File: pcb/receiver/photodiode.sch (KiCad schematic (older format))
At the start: 111 parts, among them Q201 Q_NJFET_DGS, Q202 Q_NPN_BCE, Q203 Q_NPN_BCE, Q204 Q_NPN_BCE, Q205 Q_NPN_BCE, Q206 Q_NPN_BCE, Q207 Q_NJFET_DGS, U201 ADR550ARTZ-REEL7, U202 TL974IPWR, U203 MAX4477AUA+, U204 OPA2141AIDR, U205 NLAS4599DFT2G

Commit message: Most parts footprinted; TODO analog voltage reference, photodiodes, passives
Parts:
- U202: footprint (none) -> receiver-footprints:TI-SOIC14
- U203: footprint (none) -> receiver-footprints:Maxim-uMAX8
- U204: footprint (none) -> receiver-footprints:TI-SOIC8
- U205: footprint Package_DIP:DIP-8_W7.62mm -> receiver-footprints:On-SOT363
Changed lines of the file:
@@
 F 0 "U203" H 4300 3400 50  0000 L CNN
 F 1 "MAX4477AUA+" H 4300 3000 50  0000 L CNN
-F 2 "" H 4300 3200 50  0001 C CNN
+F 2 "receiver-footprints:Maxim-uMAX8" H 4300 3200 50  0001 C CNN
 F 3 "" H 4300 3200 50  0001 C CNN
 	1    4300 3200
@@
 F 0 "U203" H 5950 3500 50  0000 L CNN
 F 1 "MAX4477AUA+" H 5950 3100 50  0000 L CNN
-F 2 "" H 5950 3300 50  0001 C CNN
+F 2 "receiver-footprints:Maxim-uMAX8" H 5950 3300 50  0001 C CNN
 F 3 "" H 5950 3300 50  0001 C CNN
 	2    5950 3300
@@
 F 0 "U204" H 8050 3600 50  0000 L CNN
 F 1 "OPA2141AIDR" H 8050 3200 50  0000 L CNN
-F 2 "" H 8050 3400 50  0001 C CNN
+F 2 "receiver-footprints:TI-SOIC8" H 8050 3400 50  0001 C CNN
 F 3 "" H 8050 3400 50  0001 C CNN
 	1    8050 3400
@@
 F 0 "U204" H 10050 3700 50  0000 L CNN
 F 1 "OPA2141AIDR" H 10050 3300 50  0000 L CNN
-F 2 "" H 10050 3500 50  0001 C CNN
+F 2 "receiver-footprints:TI-SOIC8" H 10050 3500 50  0001 C CNN
 F 3 "" H 10050 3500 50  0001 C CNN
 	2    10050 3500
@@
 F 0 "U202" H 7300 1450 50  0000 L CNN
 F 1 "TL974IPWR" H 7300 1050 50  0000 L CNN
-F 2 "" H 7250 1350 50  0001 C CNN
+F 2 "receiver-footprints:TI-SOIC14" H 7250 1350 50  0001 C CNN
 F 3 "http://www.ti.com/lit/ds/symlink/lm2902-n.pdf" H 7350 1450 50  0001 C CNN
 	1    7300 1250
@@
 F 0 "U202" H 6750 2100 50  0000 L CNN
 F 1 "TL974IPWR" H 6750 1700 50  0000 L CNN
-F 2 "" H 6700 2000 50  0001 C CNN
+F 2 "receiver-footprints:TI-SOIC14" H 6700 2000 50  0001 C CNN
 F 3 "http://www.ti.com/lit/ds/symlink/lm2902-n.pdf" H 6800 2100 50  0001 C CNN
 	2    6750 1900
@@
 F 0 "U205" H 9775 2235 50  0000 L CNN
 F 1 "NLAS4599DFT2G" H 9775 2165 50  0000 L CNN
-F 2 "Package_DIP:DIP-8_W7.62mm" H 9900 1750 50  0001 C CNN
+F 2 "receiver-footprints:On-SOT363" H 9900 1750 50  0001 C CNN
 F 3 "https://datasheets.maximintegrated.com/en/ds/DG417-DG419.pdf" H 9900 1850 50  0001 C CNN
 	1    9900 2050
@@
 F 0 "U203" H 9450 5800 50  0000 L CNN
 F 1 "MAX4477AUA+" H 9450 5400 50  0000 L CNN
-F 2 "" H 9450 5600 50  0001 C CNN
+F 2 "receiver-footprints:Maxim-uMAX8" H 9450 5600 50  0001 C CNN
 F 3 "" H 9450 5600 50  0001 C CNN
 	3    9450 5600
@@
 F 0 "U204" H 10300 5850 50  0000 L CNN
 F 1 "OPA2141AIDR" H 10300 5450 50  0000 L CNN
-F 2 "" H 10300 5650 50  0001 C CNN
+F 2 "receiver-footprints:TI-SOIC8" H 10300 5650 50  0001 C CNN
 F 3 "" H 10300 5650 50  0001 C CNN
 	3    10300 5650
@@
 F 0 "U205" H 8775 5685 50  0000 L CNN
 F 1 "NLAS4599DFT2G" H 8775 5615 50  0000 L CNN
-F 2 "Package_DIP:DIP-8_W7.62mm" H 8900 5200 50  0001 C CNN
+F 2 "receiver-footprints:On-SOT363" H 8900 5200 50  0001 C CNN
 F 3 "https://datasheets.maximintegrated.com/en/ds/DG417-DG419.pdf" H 8900 5300 50  0001 C CNN
 	2    8900 5500
@@
 F 0 "U202" H 7600 6050 50  0000 L CNN
 F 1 "TL974IPWR" H 7600 5650 50  0000 L CNN
-F 2 "" H 7550 5950 50  0001 C CNN
+F 2 "receiver-footprints:TI-SOIC14" H 7550 5950 50  0001 C CNN
 F 3 "http://www.ti.com/lit/ds/symlink/lm2902-n.pdf" H 7650 6050 50  0001 C CNN
 	5    7600 5850
@@
 F 0 "U202" H 5900 6100 50  0000 L CNN
 F 1 "TL974IPWR" H 5900 5700 50  0000 L CNN
-F 2 "" H 5850 6000 50  0001 C CNN
+F 2 "receiver-footprints:TI-SOIC14" H 5850 6000 50  0001 C CNN
 F 3 "http://www.ti.com/lit/ds/symlink/lm2902-n.pdf" H 5950 6100 50  0001 C CNN
 	4    5900 5900
@@
 F 0 "U202" H 2350 6750 50  0000 L CNN
 F 1 "TL974IPWR" H 2350 6350 50  0000 L CNN
-F 2 "" H 2300 6650 50  0001 C CNN
+F 2 "receiver-footprints:TI-SOIC14" H 2300 6650 50  0001 C CNN
 F 3 "http://www.ti.com/lit/ds/symlink/lm2902-n.pdf" H 2400 6750 50  0001 C CNN
 	3    2350 6550

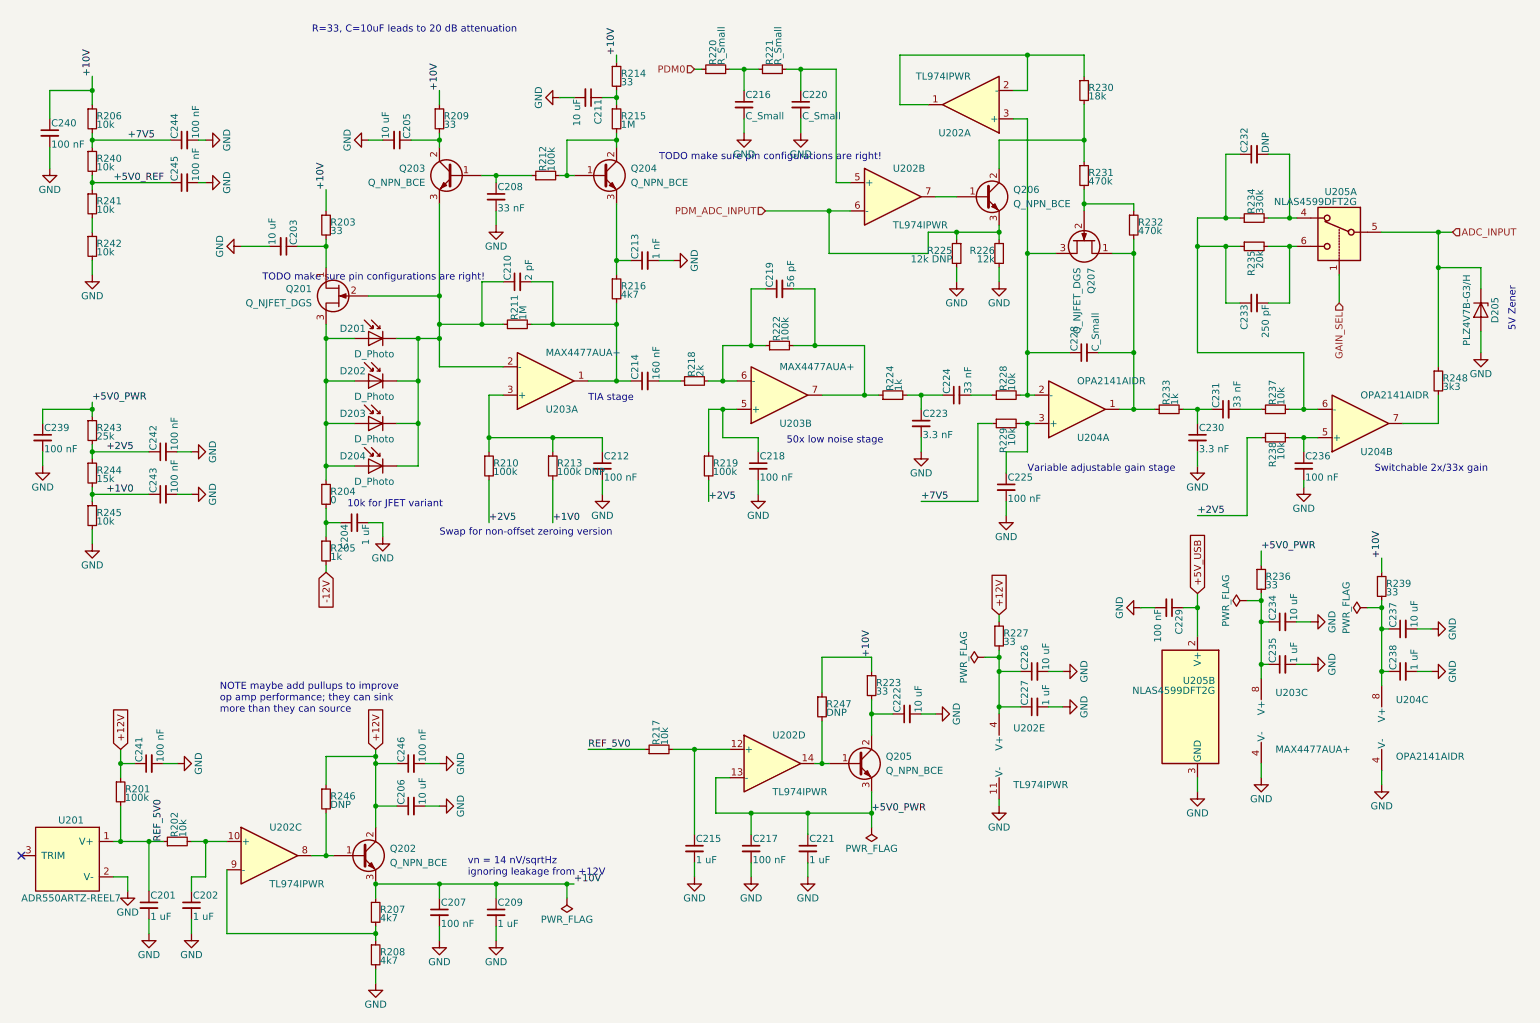
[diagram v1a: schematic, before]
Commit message: Source most passives; save before autofill
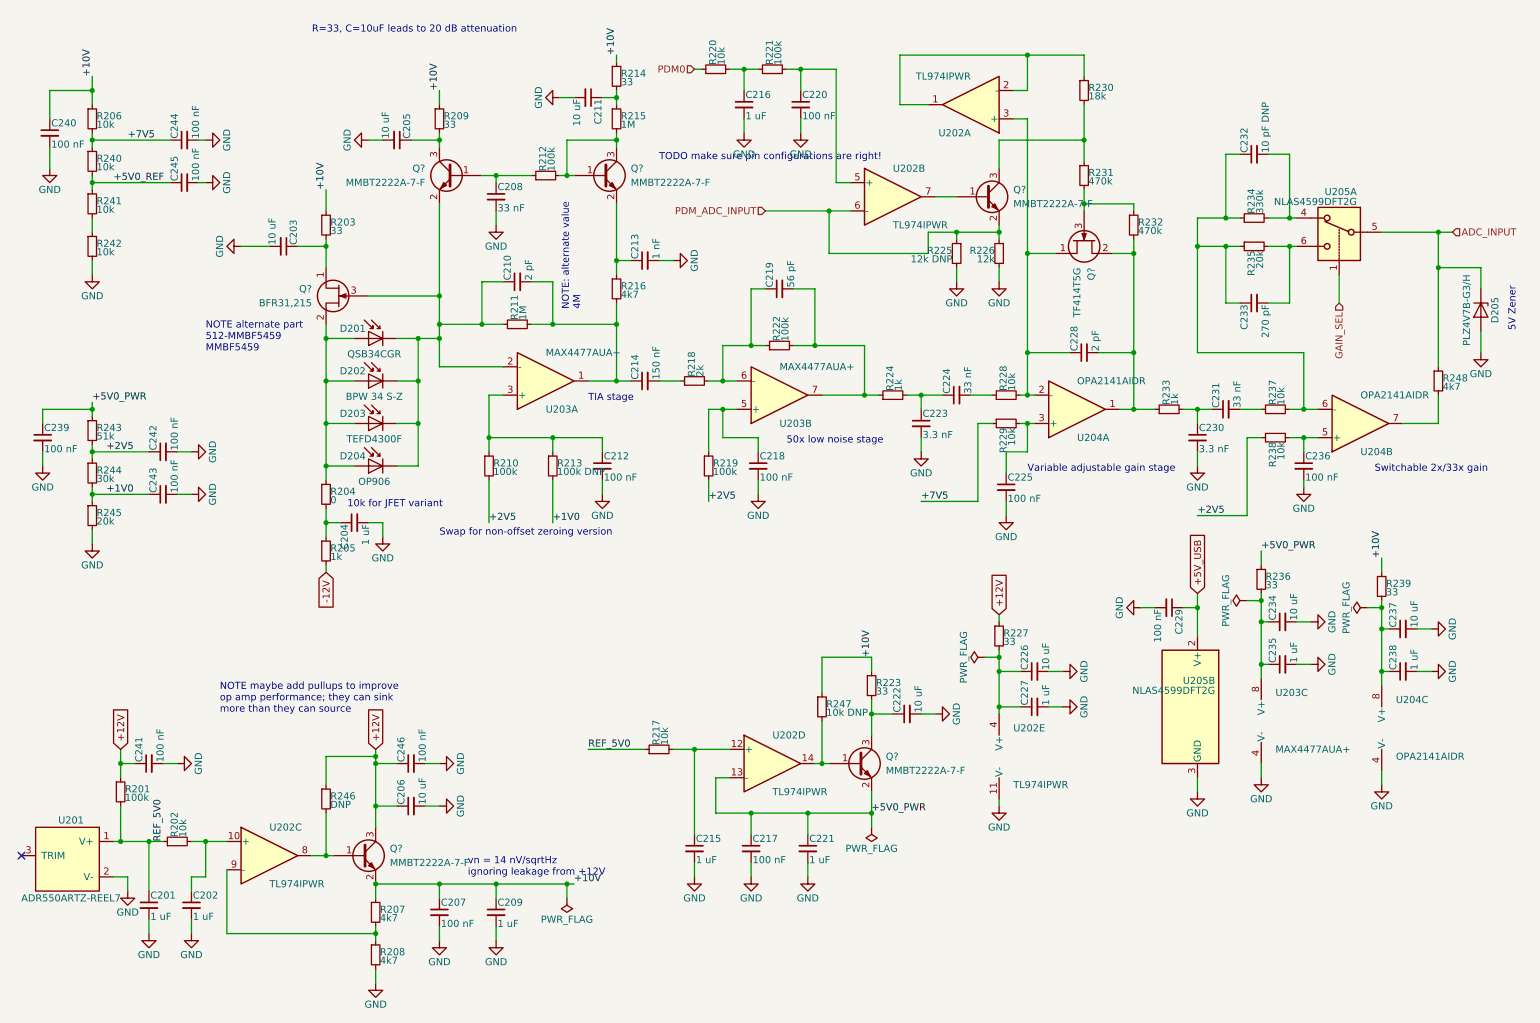
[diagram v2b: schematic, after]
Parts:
- removed Q201, Q207: Q_NJFET_DGS, symbol Device:Q_NJFET_DGS
- removed Q202, Q203, Q204, Q205, Q206: Q_NPN_BCE, symbol Device:Q_NPN_BCE
- added Q?: BFR31,215, TO_SOT_Packages_SMD:SOT-23_Handsoldering, symbol Device:Q_NJFET_DSG
- added Q?: TF414T5G, receiver-footprints:ON_XDFN3, symbol Device:Q_NJFET_SDG
- added Q? (x4): MMBT2222A-7-F, symbol Device:Q_NPN_BEC
- added Q?: MMBT2222A-7-F, TO_SOT_Packages_SMD:SOT-23_Handsoldering, symbol Device:Q_NPN_BEC
- C201: footprint (none) -> Capacitors_SMD:C_0603_HandSoldering; Mouser (none) -> 710-885012106022
- C203: footprint (none) -> Capacitors_SMD:C_0805_HandSoldering; Mouser (none) -> 81-GRM21BR61E106MA3L
- C210: footprint (none) -> Capacitors_SMD:C_0603_HandSoldering; Mouser (none) -> 603-C0603BRNPO9BN2R0
- C213: footprint (none) -> Capacitors_SMD:C_0402; Mouser (none) -> 710-885012205061
- C214: value 160 nF -> 150 nF; footprint (none) -> Capacitors_SMD:C_0603_HandSoldering; Mouser (none) -> 710-885012206021
- C216: value C_Small -> 1 uF
- C219: footprint (none) -> Capacitors_SMD:C_0402; Mouser (none) -> 77-VJ0402A560KXAPBC
- C220: value C_Small -> 100 nF
- C223: footprint (none) -> Capacitors_SMD:C_0603_HandSoldering; Mouser (none) -> 77-VJ0402A560KXAPBC
- C224: footprint (none) -> Capacitors_SMD:C_0402; Mouser (none) -> 710-885012105014
- C228: value C_Small -> 2 pF
- C232: value DNP -> 10 pF DNP
- C233: value 250 pF -> 270 pF; footprint (none) -> Capacitors_SMD:C_0402; Mouser (none) -> 963-UMK105CH271JVHF
- C240: footprint (none) -> Capacitors_SMD:C_0603_HandSoldering; Mouser (none) -> 710-885012206071
- D201: value D_Photo -> QSB34CGR; footprint (none) -> receiver-footprints:Fairchild_QSB34CGR; Mouser (none) -> 512-QSB34CGR
- D202: value D_Photo -> BPW 34 S-Z; footprint (none) -> receiver-footprints:OSRAM_BPW34S-Z; Mouser (none) -> 720-BPW34S-Z
- D203: value D_Photo -> TEFD4300F; footprint (none) -> LEDs:LED_D3.0mm; Mouser (none) -> 78-TEFD4300F
- D204: value D_Photo -> OP906; footprint (none) -> LEDs:LED_D3.0mm; Mouser (none) -> 828-OP906
- R201: footprint (none) -> Resistors_SMD:R_0402; Mouser (none) -> 603-RC0402JR-13100KL
- R203: footprint (none) -> Resistors_SMD:R_0603_HandSoldering; Mouser (none) -> 755-ESR03EZPJ330
- R204: footprint (none) -> Resistors_SMD:R_0603_HandSoldering; Mouser (none) -> 755-SFR03EZPJ000
- R205: footprint (none) -> Resistors_SMD:R_0603_HandSoldering; Mouser (none) -> 603-RC0603JR-071KL
- R206: footprint (none) -> Resistors_SMD:R_0603_HandSoldering; Mouser (none) -> 603-RC0603FR-0710KL
- R207: footprint (none) -> Resistors_SMD:R_0603_HandSoldering; Mouser (none) -> 71-CRCW06034K70JNEAC
- R211: footprint (none) -> Resistors_SMD:R_0603_HandSoldering; Mouser (none) -> 603-RC0603JR-071ML
- R218: footprint (none) -> Resistors_SMD:R_0603_HandSoldering; Mouser (none) -> 603-RC0603FR-102KL
- R220: value R_Small -> 10k
- R221: value R_Small -> 100k
- R226: footprint (none) -> Resistors_SMD:R_0603_HandSoldering; Mouser (none) -> 603-RC0603FR-1012KL
- R230: footprint (none) -> Resistors_SMD:R_0603_HandSoldering; Mouser (none) -> 603-RC0603FR-0718KL
- R231: footprint (none) -> Resistors_SMD:R_0603_HandSoldering; Mouser (none) -> 603-RC0603FR-07470KL
- R234: footprint (none) -> Resistors_SMD:R_0402; Mouser (none) -> 603-RC0402FR-07330KL
- R243: value 25k -> 51k; footprint (none) -> Resistors_SMD:R_0402; Mouser (none) -> 603-RC0402FR-0751KL
- R244: value 15k -> 30k; footprint (none) -> Resistors_SMD:R_0402; Mouser (none) -> 603-AC0402FR-0730KL
- R245: value 10k -> 20k; footprint (none) -> Resistors_SMD:R_0402; Mouser (none) -> 755-SFR01MZPF2002
- R247: value DNP -> 10k DNP
- R248: value 3k3 -> 4k7
- U201: footprint (none) -> TO_SOT_Packages_SMD:SOT-23_Handsoldering
- U202: Mouser (none) -> 595-TL974IPWR
- U203: Mouser (none) -> 700-MAX4477AUA
- U204: Mouser (none) -> 595-OPA2141AIDR
- U205: Mouser (none) -> 863-NLAS4599DFT2G
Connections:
- net +10V: now also Q?.2 (E)
- net +12V: now also Q?.3 (C)
- net +5V0_PWR: now also Q?.2 (E)
- net PDM_ADC_INPUT: now also Q?.2 (E)
- net at C210.1, D201.1 (K), D202.1 (K)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: now also Q?.2 (E), Q?.3 (G)
- net at C208.1, R212.1: now also Q?.1 (B)
- net at C205.1, R209.2: now also Q?.3 (C)
- net at R212.2, R215.2: now also Q?.1 (B), Q?.3 (C)
- net at C213.1, R216.1: now also Q?.2 (E)
- net at C203.1, R203.2: now also Q?.1 (D)
- net at D201.2 (A), D202.2 (A), D203.2 (A)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: now also Q?.2 (S)
- net at C228.2, R232.2, R233.1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: now also Q?.2 (D)
- net at C228.1, R228.2, U202.3 (+)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: now also Q?.1 (S)
- net at R231.2, R232.1: now also Q?.3 (G)
- net at R230.2, R231.1: now also Q?.3 (C)
- net at U202.7: now also Q?.1 (B)
- net at R246.2, U202.8: now also Q?.1 (B)
- net at R247.2, U202.14: now also Q?.1 (B)
- net at C222.1, R223.2: now also Q?.3 (C)
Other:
- note added: "NOTE alternate part\n512-MMBF5459\nMMBF5459"
- note added: "NOTE: alternate value\n4M"

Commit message: Autofill components
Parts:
- C202, C204, C209, C215, C216, C221, C227, C235, C238: footprint (none) -> Capacitors_SMD:C_0603_HandSoldering; Mouser (none) -> 710-885012106022
- C205, C206, C211, C222, C226, C234, C237: footprint (none) -> Capacitors_SMD:C_0805_HandSoldering; Mouser (none) -> 81-GRM21BR61E106MA3L
- C207, C212, C217, C218, C220, C225, C229, C236, C239, C241, C242, C243, C244, C245, C246: footprint (none) -> Capacitors_SMD:C_0603_HandSoldering; Mouser (none) -> 710-885012206071
- C208, C231: footprint (none) -> Capacitors_SMD:C_0402; Mouser (none) -> 710-885012105014
- C228: footprint (none) -> Capacitors_SMD:C_0603_HandSoldering; Mouser (none) -> 603-C0603BRNPO9BN2R0
- C230: footprint (none) -> Capacitors_SMD:C_0603_HandSoldering; Mouser (none) -> 77-VJ0402A560KXAPBC
- Q? (x4): footprint (none) -> TO_SOT_Packages_SMD:SOT-23_Handsoldering; Mouser (none) -> 621-MMBT2222A-F
- R202, R217, R220, R228, R229, R237, R238, R240, R241, R242: footprint (none) -> Resistors_SMD:R_0603_HandSoldering; Mouser (none) -> 603-RC0603FR-0710KL
- R208, R216, R248: footprint (none) -> Resistors_SMD:R_0603_HandSoldering; Mouser (none) -> 71-CRCW06034K70JNEAC
- R209, R214, R223, R227, R236, R239: footprint (none) -> Resistors_SMD:R_0603_HandSoldering; Mouser (none) -> 755-ESR03EZPJ330
- R210, R212, R219, R221, R222: footprint (none) -> Resistors_SMD:R_0402; Mouser (none) -> 603-RC0402JR-13100KL
- R215: footprint (none) -> Resistors_SMD:R_0603_HandSoldering; Mouser (none) -> 603-RC0603JR-071ML
- R224, R233: footprint (none) -> Resistors_SMD:R_0603_HandSoldering; Mouser (none) -> 603-RC0603JR-071KL
- R232: footprint (none) -> Resistors_SMD:R_0603_HandSoldering; Mouser (none) -> 603-RC0603FR-07470KL
- R235: footprint (none) -> Resistors_SMD:R_0402; Mouser (none) -> 755-SFR01MZPF2002
- U202: Mouser (none) -> 595-TL974IPWR
- U203: Mouser (none) -> 700-MAX4477AUA
- U204: Mouser (none) -> 595-OPA2141AIDR
- U205: Mouser (none) -> 863-NLAS4599DFT2G

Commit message: Footprint more stuff
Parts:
- C232: value 10 pF DNP -> 10 pF
- D205: footprint (none) -> receiver-footprints:Vishay_DO-219AC; Mouser (none) -> 78-PLZ4V7B-G3/H
- R213: value 100k DNP -> 100k
- R225: value 12k DNP -> 12k
- R246: value DNP -> 1k
- R247: value 10k DNP -> 10k
- U201: Mouser (none) -> 584-ADR550ARTZ-R7
- gave numbers to parts that had none: 7
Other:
- note added: "DNP"
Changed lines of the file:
@@
 P 7200 2300
 F 0 "R225" H 7230 2320 50  0000 L CNN
-F 1 "12k DNP" H 7230 2260 50  0000 L CNN
+F 1 "12k" H 7230 2260 50  0000 L CNN
 F 2 "" H 7200 2300 50  0001 C CNN
 F 3 "~" H 7200 2300 50  0001 C CNN
@@
 P 9300 1600
 F 0 "C232" H 9310 1670 50  0000 L CNN
-F 1 "10 pF DNP" H 9310 1520 50  0000 L CNN
+F 1 "10 pF" H 9310 1520 50  0000 L CNN
 F 2 "" H 9300 1600 50  0001 C CNN
 F 3 "~" H 9300 1600 50  0001 C CNN
@@
 P 4350 3800
 F 0 "R213" H 4380 3820 50  0000 L CNN
-F 1 "100k DNP" H 4380 3760 50  0000 L CNN
+F 1 "100k" H 4380 3760 50  0000 L CNN
 F 2 "" H 4350 3800 50  0001 C CNN
 F 3 "~" H 4350 3800 50  0001 C CNN
@@
 F 2 "TO_SOT_Packages_SMD:SOT-23_Handsoldering" H 950 6550 50  0001 C CNN
 F 3 "" H 950 6550 50  0001 C CNN
+F 4 "584-ADR550ARTZ-R7" H 950 6550 50  0001 C CNN "Mouser"
 	1    950  6550
 	-1   0    0    -1
@@
 P 2750 6150
 F 0 "R246" H 2780 6170 50  0000 L CNN
-F 1 "DNP" H 2780 6110 50  0000 L CNN
+F 1 "1k" H 2780 6110 50  0000 L CNN
 F 2 "" H 2750 6150 50  0001 C CNN
 F 3 "~" H 2750 6150 50  0001 C CNN
@@
 P 6250 5500
 F 0 "R247" H 6280 5520 50  0000 L CNN
-F 1 "10k DNP" H 6280 5460 50  0000 L CNN
+F 1 "10k" H 6280 5460 50  0000 L CNN
 F 2 "" H 6250 5500 50  0001 C CNN
 F 3 "~" H 6250 5500 50  0001 C CNN
@@
 F 0 "D205" H 10900 2800 50  0000 C CNN
 F 1 "PLZ4V7B-G3/H" H 10900 2600 50  0000 C CNN
-F 2 "" H 10900 2700 50  0001 C CNN
+F 2 "receiver-footprints:Vishay_DO-219AC" H 10900 2700 50  0001 C CNN
 F 3 "~" H 10900 2700 50  0001 C CNN
+F 4 "78-PLZ4V7B-G3/H" H 10900 2700 50  0001 C CNN "Mouser"
 	1    10900 2700
 	0    1    1    0
@@
 	7500 5150 7500 5250
 $Comp
-L Device:Q_NJFET_DSG Q?
+L Device:Q_NJFET_DSG Q201
 U 1 1 5C636C60
 P 2850 2600
-F 0 "Q?" H 3050 2650 50  0000 L CNN
+F 0 "Q201" H 3050 2650 50  0000 L CNN
 F 1 "BFR31,215" H 3050 2550 50  0000 L CNN
 F 2 "TO_SOT_Packages_SMD:SOT-23_Handsoldering" H 3050 2700 50  0001 C CNN
@@
 $EndComp
 $Comp
-L Device:Q_NJFET_SDG Q?
+L Device:Q_NJFET_SDG Q207
 U 1 1 5C65B0BB
 P 8100 2200
-F 0 "Q?" H 8300 2250 50  0000 L CNN
+F 0 "Q207" H 8300 2250 50  0000 L CNN
 F 1 "TF414T5G" H 8300 2150 50  0000 L CNN
 F 2 "receiver-footprints:ON_XDFN3" H 8300 2300 50  0001 C CNN
@@
 NOTE alternate part\n512-MMBF5459\nMMBF5459
 $Comp
-L Device:Q_NPN_BEC Q?
+L Device:Q_NPN_BEC Q204
 U 1 1 5C66871D
 P 4700 1750
-F 0 "Q?" H 4900 1800 50  0000 L CNN
+F 0 "Q204" H 4900 1800 50  0000 L CNN
 F 1 "MMBT2222A-7-F" H 4900 1700 50  0000 L CNN
 F 2 "TO_SOT_Packages_SMD:SOT-23_Handsoldering" H 4900 1850 50  0001 C CNN
@@
 $EndComp
 $Comp
-L Device:Q_NPN_BEC Q?
+L Device:Q_NPN_BEC Q203
 U 1 1 5C668A80
 P 3650 1750
-F 0 "Q?" H 3850 1800 50  0000 L CNN
+F 0 "Q203" H 3850 1800 50  0000 L CNN
 F 1 "MMBT2222A-7-F" H 3850 1700 50  0000 L CNN
 F 2 "TO_SOT_Packages_SMD:SOT-23_Handsoldering" H 3850 1850 50  0001 C CNN
@@
 $EndComp
 $Comp
-L Device:Q_NPN_BEC Q?
+L Device:Q_NPN_BEC Q206
 U 1 1 5C668C90
 P 7400 1900
-F 0 "Q?" H 7600 1950 50  0000 L CNN
+F 0 "Q206" H 7600 1950 50  0000 L CNN
 F 1 "MMBT2222A-7-F" H 7600 1850 50  0000 L CNN
 F 2 "TO_SOT_Packages_SMD:SOT-23_Handsoldering" H 7600 2000 50  0001 C CNN
@@
 $EndComp
 $Comp
-L Device:Q_NPN_BEC Q?
+L Device:Q_NPN_BEC Q205
 U 1 1 5C66B190
 P 6500 5900
-F 0 "Q?" H 6700 5950 50  0000 L CNN
+F 0 "Q205" H 6700 5950 50  0000 L CNN
 F 1 "MMBT2222A-7-F" H 6700 5850 50  0000 L CNN
 F 2 "TO_SOT_Packages_SMD:SOT-23_Handsoldering" H 6700 6000 50  0001 C CNN
@@
 $EndComp
 $Comp
-L Device:Q_NPN_BEC Q?
+L Device:Q_NPN_BEC Q202
 U 1 1 5C66B3BA
 P 3000 6550
-F 0 "Q?" H 3200 6600 50  0000 L CNN
+F 0 "Q202" H 3200 6600 50  0000 L CNN
 F 1 "MMBT2222A-7-F" H 3200 6500 50  0000 L CNN
 F 2 "TO_SOT_Packages_SMD:SOT-23_Handsoldering" H 3200 6650 50  0001 C CNN
@@
 Text Notes 4550 2700 1    50   ~ 0
 NOTE: alternate value\n4M
+Text Notes 6950 2450 0    50   ~ 0
+DNP
+Text Notes 9250 1300 0    50   ~ 0
+DNP
+Text Notes 4450 4000 0    50   ~ 0
+DNP
+Text Notes 2600 6200 0    50   ~ 0
+DNP
+Text Notes 6050 5550 0    50   ~ 0
+DNP
 $EndSCHEMATC
